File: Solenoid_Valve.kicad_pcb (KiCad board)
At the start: 2 copper layers, 85.9 x 50 mm, 62 parts, among them IC1 Si8621AB-B-ISR, J1 Bus_mechaken_PCIexpress_x16_1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, J10 Conn_01x02, J11 Conn_01x02, J12 Conn_01x02, J13 Conn_01x02, J14 Conn_01x02, J15 Conn_01x02, J16 Conn_01x02, J17 Conn_01x02, J18 Conn_01x02, J19 Conn_01x02, J2 Conn_01x05, J20 Conn_01x02, J3 Conn_01x02, J4 Conn_01x02, J5 Conn_01x02, J6 Conn_01x02, J7 Conn_01x03, J8 Conn_01x02, J9 Conn_01x02, Q1 ULN2004D1013TR, Q2 ULN2004D1013TR, Q3 ULN2004D1013TR, SW1 SW_Push, U1 LDL1117S33R, U2 STM32F042K6Tx, U3 MCP2562-E-SN, U4 L7812, U5 LDL1117S33R

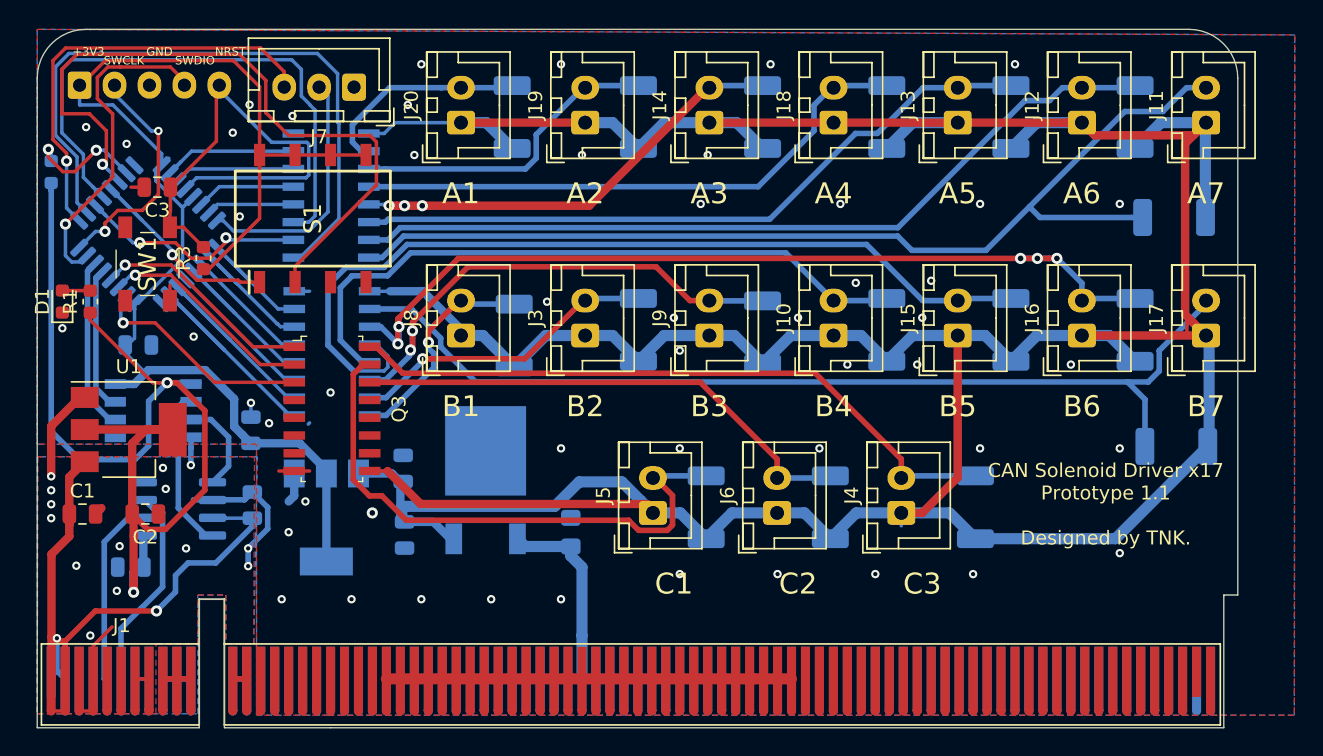
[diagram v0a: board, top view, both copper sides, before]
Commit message: change
Remove NRST SW
clean
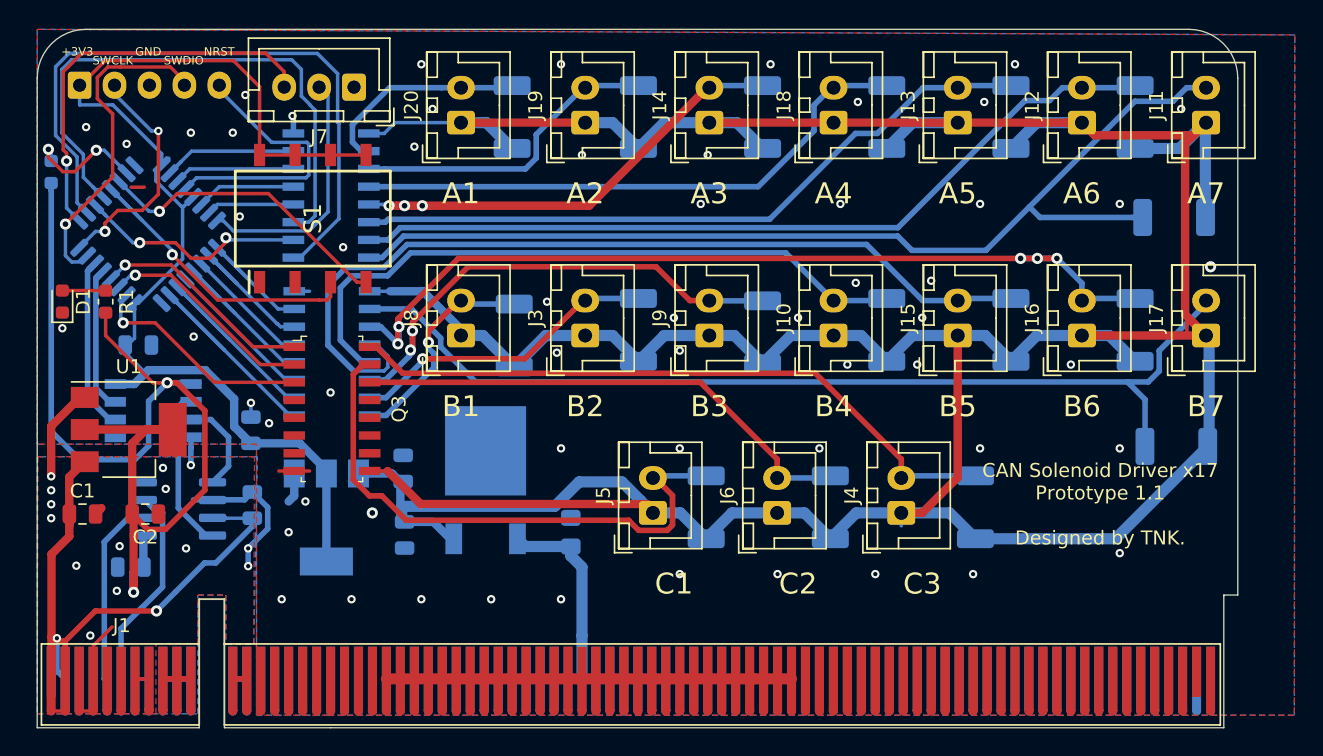
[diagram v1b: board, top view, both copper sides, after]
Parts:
- removed C3: 0.1uF, Capacitor_SMD:C_0805_2012Metric
- removed R3: 10K, Resistor_SMD:R_0603_1608Metric
- removed SW1: SW_Push, SamacSys_Parts:PTS647SM38SMTR2LFS
- moved R1 1.10 mm to (154.9, 119.5)
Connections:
- S1 pad 1: DIP_SW_1 -> (no net)
- S1 pad 2: DIP_SW_2 -> (no net)
- S1 pad 3: (no net) -> DIP_SW_1
- S1 pad 4: (no net) -> DIP_SW_2
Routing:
- net DIP_SW_2: track 50.5 -> 21.8 mm
- net NRST: track 34.4 -> 20.3 mm
- net 3.3V: track 94.1 -> 84.1 mm
- net DIP_SW_1: track 16.7 -> 23.5 mm
- net VCP_RX: track 31.0 -> 29.2 mm
- net Net-(D1-Pad2): track 2.01 -> 3.11 mm
- net +5V: track 59.3 -> 58.6 mm
- net GNDPWR: vias 51 -> 58
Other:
- board text added: "VCP_TX"
- board text added: "VXP_TX"

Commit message: fix
ST-LINK部分の配線を修正
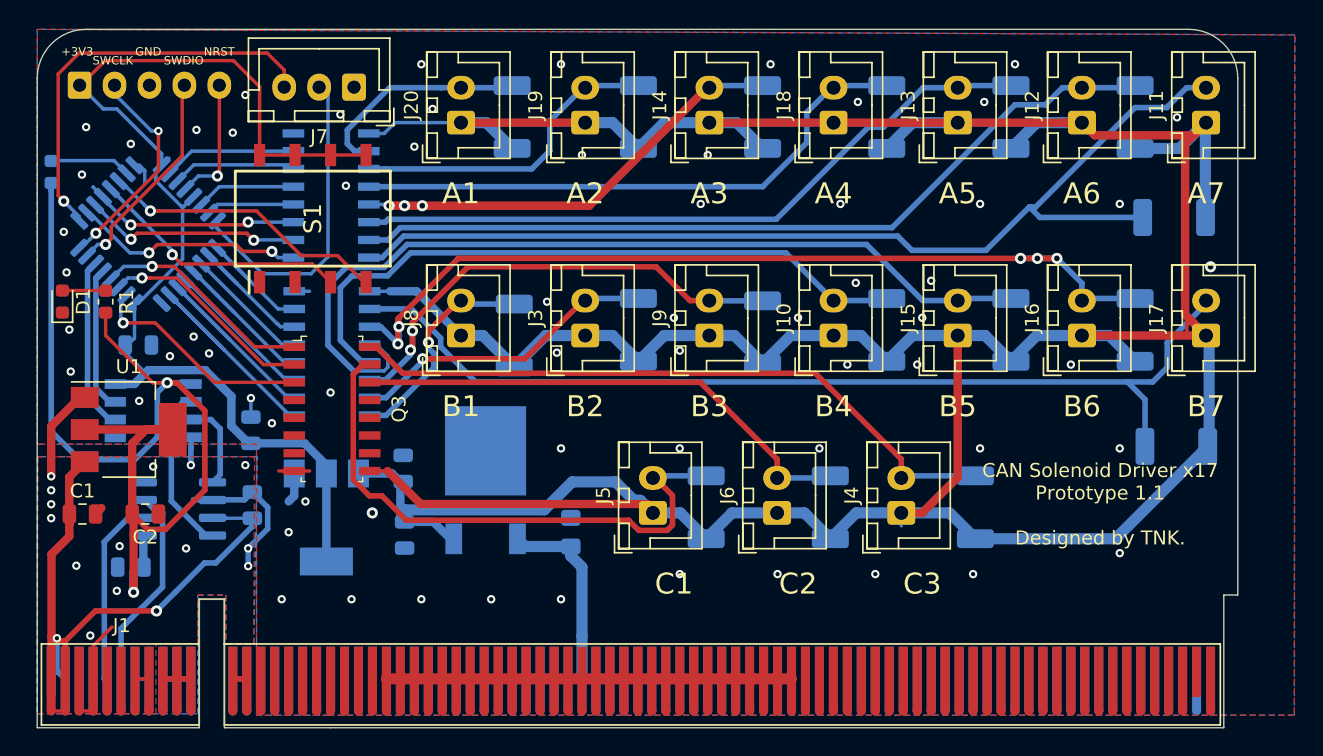
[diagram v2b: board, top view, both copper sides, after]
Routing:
- net IC_B1: track 47.4 -> 17.1 mm, vias 0 -> 2
- net IC_B3: track 41.6 -> 15.6 mm, vias 0 -> 2
- net NRST: track 20.3 -> 10.1 mm, vias 0 -> 1
- net /SWDIO: track 23.8 -> 15.4 mm
- net VCP_TX: track 18.0 -> 22.8 mm
- net /BOOT: track 8.84 -> 5.77 mm, vias 2 -> 0
- net DIP_SW_1: track 23.5 -> 21.8 mm
- net 3.3V: track 84.1 -> 82.5 mm
- net /SWCLK: track 17.0 -> 15.7 mm
- net IC_B2: track 17.6 -> 16.4 mm
- net DIP_SW_2: track 21.8 -> 20.8 mm
- net +12V: track 366.6 -> 365.9 mm
- net Solenoid_B7: track 15.3 -> 15.9 mm
- net GNDPWR: track 11.1 -> 10.7 mm, vias 58 -> 64

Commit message: fix
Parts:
- J1: footprint PCIe:BUS_mechaken_PCIexpress_x16_164_Position -> PCIe:BUS_mechaken_PCIexpress_x16
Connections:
- Q3 pad 10: (no net) -> Net-(Q3-Pad10)
- Q3 pad 11: (no net) -> Net-(Q3-Pad11)
- Q3 pad 12: (no net) -> Net-(Q3-Pad12)
- Q3 pad 13: (no net) -> Net-(Q3-Pad13)
- Q3 pad 4: (no net) -> Net-(Q3-Pad4)
- Q3 pad 5: (no net) -> Net-(Q3-Pad5)
- Q3 pad 6: (no net) -> Net-(Q3-Pad6)
- Q3 pad 7: (no net) -> Net-(Q3-Pad7)
- S1 pad 1: (no net) -> Net-(S1-Pad1)
- S1 pad 2: (no net) -> Net-(S1-Pad2)
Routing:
- net +12V: track 365.9 -> 314.8 mm
- net +5V: track 58.6 -> 46.5 mm
- net GND: track 27.1 -> 21.6 mm
- net Net-(J1-PadB5): track 5.60 -> 1.00 mm
- net Net-(J1-PadA5): track 5.60 -> 1.00 mm
- net CAN-: track 15.8 -> 13.3 mm
- net VCC: track 45.4 -> 42.9 mm
- net Net-(J1-PadB6): track 4.30 -> 2.00 mm
- net Net-(J1-PadB4): track 2.30 -> 0.00 mm
- net Net-(J1-PadB3): track 2.30 -> 0.00 mm
- net CAN+: track 17.4 -> 15.1 mm
- net Net-(J1-PadA6): track 4.30 -> 2.00 mm
- net Solenoid_C2: track 41.7 -> 42.8 mm
- net GNDPWR: track 10.7 -> 11.5 mm, vias 64 -> 62
- net +3V3: track 82.4 -> 83.2 mm
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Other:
- board size 85.9 x 50 mm -> 85.6 x 41.1 mm

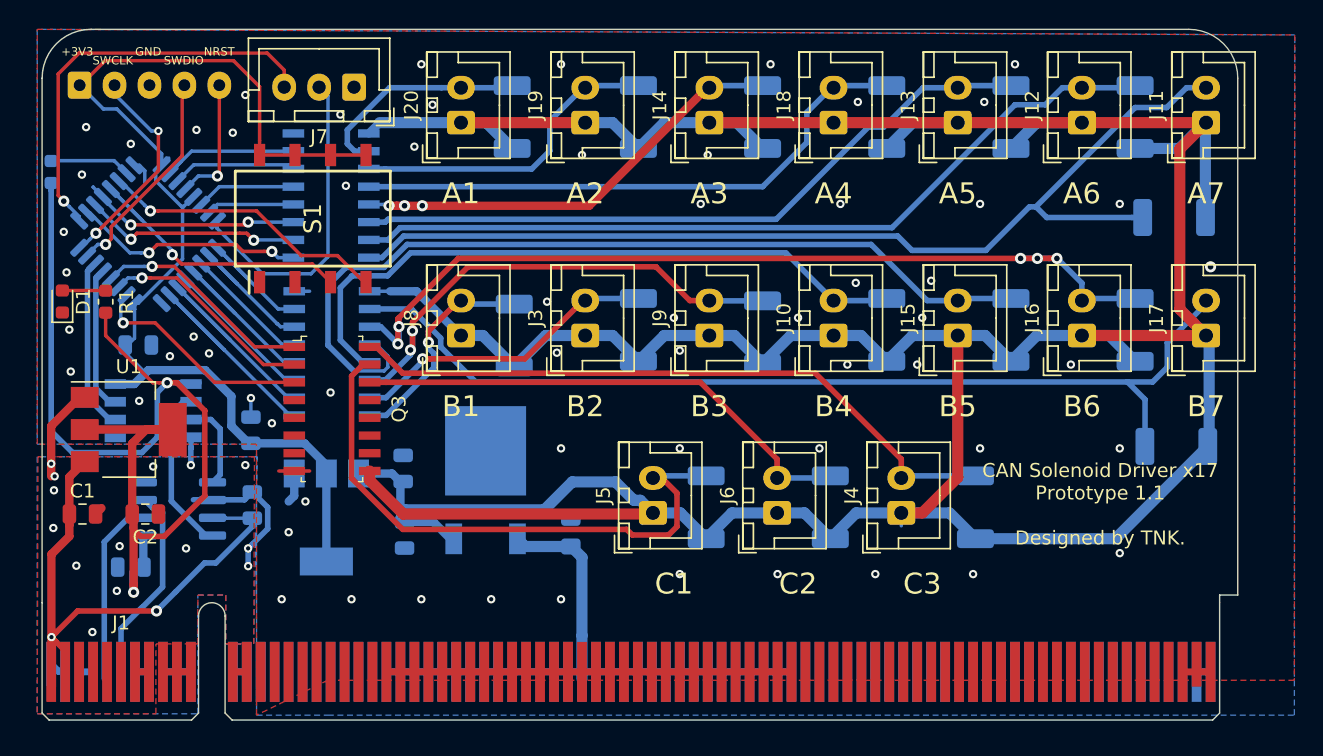
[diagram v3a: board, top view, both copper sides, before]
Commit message: fix
BOOT0の配線を修正
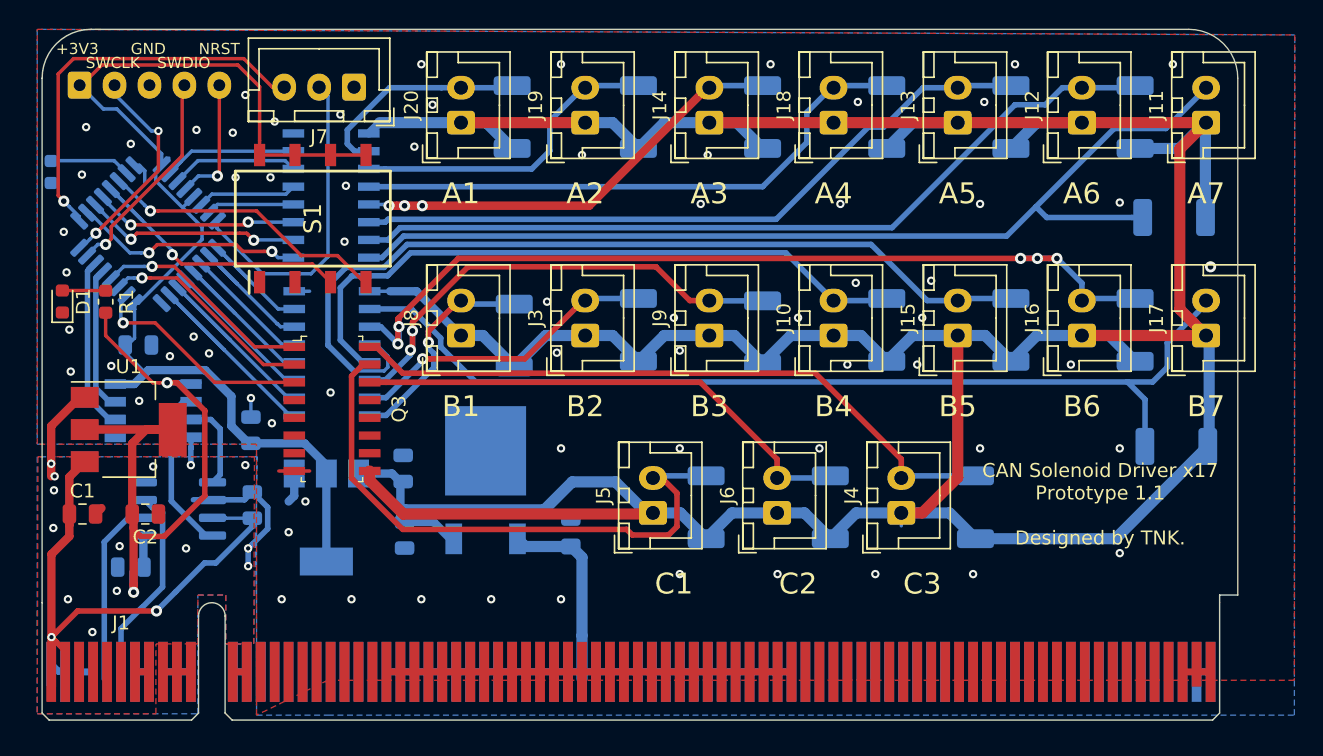
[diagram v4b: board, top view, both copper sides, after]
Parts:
- C7: value 1uF -> 0.33uF
- C8: value 4.7uF -> 0.1uF
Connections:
- R2 pad 2: +3V3 -> GNDPWR
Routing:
- net +3V3: track 83.2 -> 52.5 mm
- net VCP_RX: track 29.6 -> 28.6 mm
- net IC_B3: track 15.6 -> 14.6 mm
- net Solenoid_B1: track 73.8 -> 73.0 mm
- net 3.3V: track 82.5 -> 83.2 mm
- net GNDPWR: vias 62 -> 68

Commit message: change
フットプリントを手はんだ用に変更
レギュレーター保護用のダイオードを追加
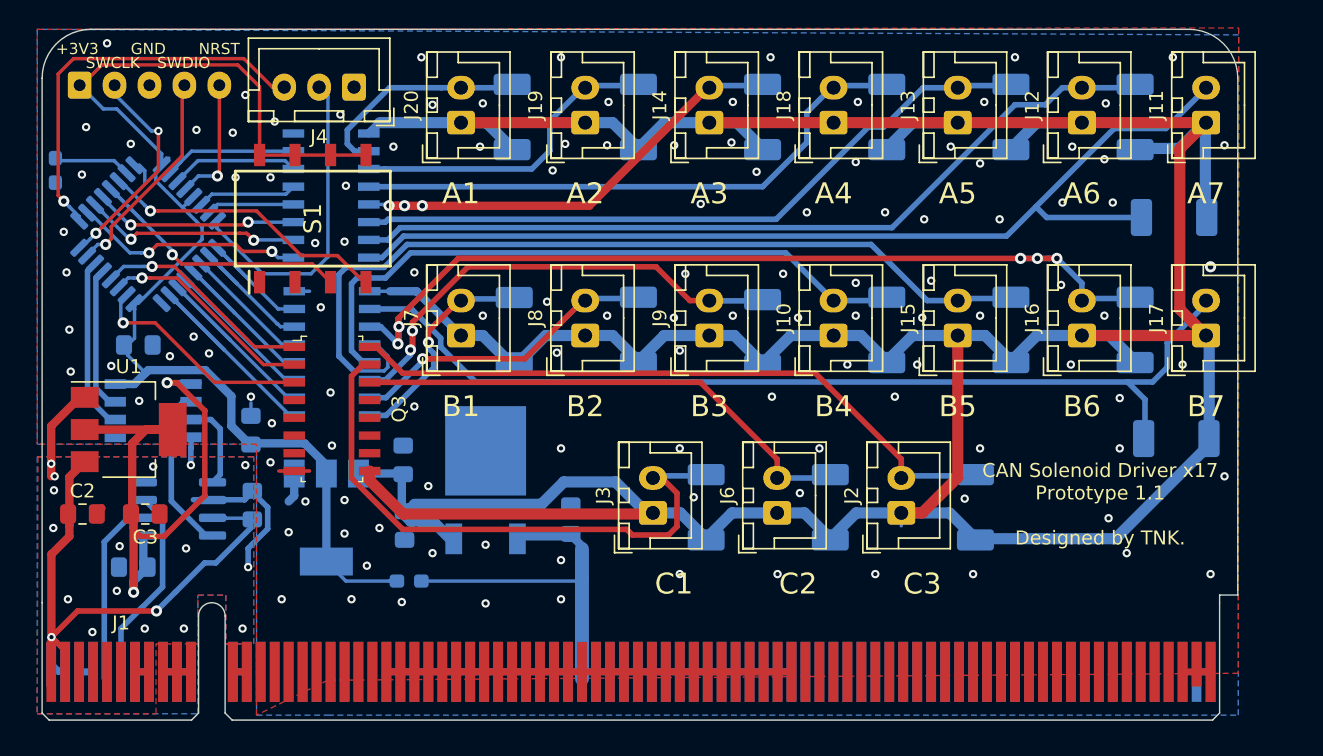
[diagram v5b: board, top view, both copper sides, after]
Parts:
- removed the D1 at (151.8, 119.5)
- removed the R1 at (154.9, 119.5)
- added D18: D_Schottky, Diode_SMD:D_0603_1608Metric_Pad1.05x0.95mm_HandSolder, B.Cu at (176.6, 139.5)
- C1: renamed from C5; footprint Capacitor_SMD:C_0805_2012Metric -> Capacitor_SMD:C_0805_2012Metric_Pad1.15x1.40mm_HandSolder
- C2: renamed from C1; footprint Capacitor_SMD:C_0805_2012Metric -> Capacitor_SMD:C_0805_2012Metric_Pad1.15x1.40mm_HandSolder
- C3: renamed from C2; footprint Capacitor_SMD:C_0805_2012Metric -> Capacitor_SMD:C_0805_2012Metric_Pad1.15x1.40mm_HandSolder
- C4: renamed from C6; footprint Capacitor_SMD:C_0805_2012Metric -> Capacitor_SMD:C_0805_2012Metric_Pad1.15x1.40mm_HandSolder
- C5: renamed from C9; footprint Capacitor_SMD:C_0805_2012Metric -> Capacitor_SMD:C_0805_2012Metric_Pad1.15x1.40mm_HandSolder
- C6: renamed from C4; footprint Capacitor_SMD:C_0805_2012Metric -> Capacitor_SMD:C_0805_2012Metric_Pad1.15x1.40mm_HandSolder
- C7: renamed from C10; footprint Capacitor_SMD:C_0805_2012Metric -> Capacitor_SMD:C_0805_2012Metric_Pad1.15x1.40mm_HandSolder
- C9: renamed from C8; footprint Capacitor_SMD:C_0805_2012Metric -> Capacitor_SMD:C_0805_2012Metric_Pad1.15x1.40mm_HandSolder
- D1: renamed from D2; footprint Diode_SMD:D_2010_5025Metric -> Diode_SMD:D_2010_5025Metric_Pad1.52x2.65mm_HandSolder
- D10: renamed from D12; footprint Diode_SMD:D_2010_5025Metric -> Diode_SMD:D_2010_5025Metric_Pad1.52x2.65mm_HandSolder
- D11: renamed from D13; footprint Diode_SMD:D_2010_5025Metric -> Diode_SMD:D_2010_5025Metric_Pad1.52x2.65mm_HandSolder
- D12: renamed from D14; footprint Diode_SMD:D_2010_5025Metric -> Diode_SMD:D_2010_5025Metric_Pad1.52x2.65mm_HandSolder
- D13: renamed from D15; footprint Diode_SMD:D_2010_5025Metric -> Diode_SMD:D_2010_5025Metric_Pad1.52x2.65mm_HandSolder
- D14: renamed from D16; footprint Diode_SMD:D_2010_5025Metric -> Diode_SMD:D_2010_5025Metric_Pad1.52x2.65mm_HandSolder
- D15: renamed from D17; footprint Diode_SMD:D_2010_5025Metric -> Diode_SMD:D_2010_5025Metric_Pad1.52x2.65mm_HandSolder
- D16: renamed from D18; footprint Diode_SMD:D_2010_5025Metric -> Diode_SMD:D_2010_5025Metric_Pad1.52x2.65mm_HandSolder
- D17: renamed from D19; footprint Diode_SMD:D_2010_5025Metric -> Diode_SMD:D_2010_5025Metric_Pad1.52x2.65mm_HandSolder
- D2: renamed from D3; footprint Diode_SMD:D_2010_5025Metric -> Diode_SMD:D_2010_5025Metric_Pad1.52x2.65mm_HandSolder
- D3: renamed from D4; footprint Diode_SMD:D_2010_5025Metric -> Diode_SMD:D_2010_5025Metric_Pad1.52x2.65mm_HandSolder
- D4: renamed from D6; footprint Diode_SMD:D_2010_5025Metric -> Diode_SMD:D_2010_5025Metric_Pad1.52x2.65mm_HandSolder
- D5: renamed from D7; footprint Diode_SMD:D_2010_5025Metric -> Diode_SMD:D_2010_5025Metric_Pad1.52x2.65mm_HandSolder
- D6: renamed from D8; footprint Diode_SMD:D_2010_5025Metric -> Diode_SMD:D_2010_5025Metric_Pad1.52x2.65mm_HandSolder
- D7: renamed from D9; footprint Diode_SMD:D_2010_5025Metric -> Diode_SMD:D_2010_5025Metric_Pad1.52x2.65mm_HandSolder
- D8: renamed from D10; footprint Diode_SMD:D_2010_5025Metric -> Diode_SMD:D_2010_5025Metric_Pad1.52x2.65mm_HandSolder
- D9: renamed from D11; footprint Diode_SMD:D_2010_5025Metric -> Diode_SMD:D_2010_5025Metric_Pad1.52x2.65mm_HandSolder
- R1: renamed from R2; footprint Resistor_SMD:R_0603_1608Metric -> Resistor_SMD:R_0603_1608Metric_Pad1.05x0.95mm_HandSolder
- U5: renamed from U4; value L7812 -> NJM7812
- moved C8 0.90 mm to (188.2, 135.1)
- moved C9 0.67 mm to (176.3, 135.5)
- moved C5 0.61 mm to (176.2, 130.8)
- moved D14 0.56 mm to (231.6, 129.3)
- moved D4 0.38 mm to (184.2, 121.5)
- moved R1 0.32 mm to (151.3, 110.1)
- moved C1 0.18 mm to (156.9, 138.5)
- renumbered C7 to C8, J4 to J2, J5 to J3, J7 to J4, J2 to J5, J8 to J7, J3 to J8, U3 to U2, U2 to U3, U5 to U4
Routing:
- net VCC: track 42.9 -> 55.3 mm
- net +3V3: track 52.5 -> 45.4 mm
- net 3.3V: track 83.2 -> 88.8 mm
- net Net-(D1-Pad2): track 3.11 -> 0.00 mm
- net Solenoid_A4: track 48.4 -> 47.0 mm
- net +12V: track 314.8 -> 313.9 mm
- net Solenoid_A5: track 63.7 -> 63.0 mm
- net GNDPWR: vias 68 -> 120
- net GND: vias 14 -> 16
